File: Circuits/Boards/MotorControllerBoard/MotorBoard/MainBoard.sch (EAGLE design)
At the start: 90 parts, among them M1 IRFS7537PBF, M2 IRFS7537PBF, M3 IRFS7537PBF, M4 IRFS7537PBF, M5 IRFS7537PBF, M6 IRFS7537PBF, M7 IRFS7537PBF, M8 IRFS7537PBF, Q1 2N3904, Q10 2N3904, Q11 2N3904, Q12 2N3904, Q13 2N3904, Q14 2N3904, Q15 2N3904, Q16 2N3904, Q2 2N3904, Q3 2N3904, Q4 2N3904, Q5 2N3904, Q6 2N3904, Q7 2N3904, Q8 2N3904, Q9 2N3904

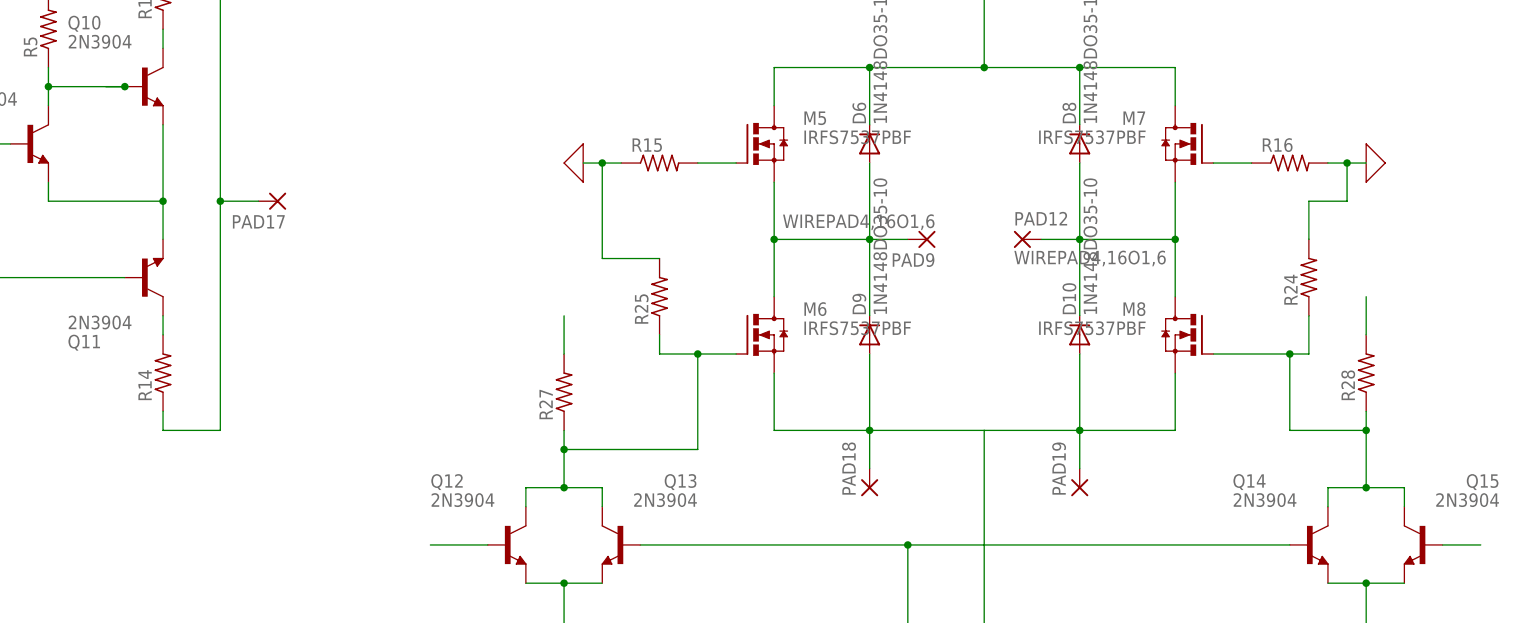
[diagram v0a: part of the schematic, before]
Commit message: Single board, two motor update
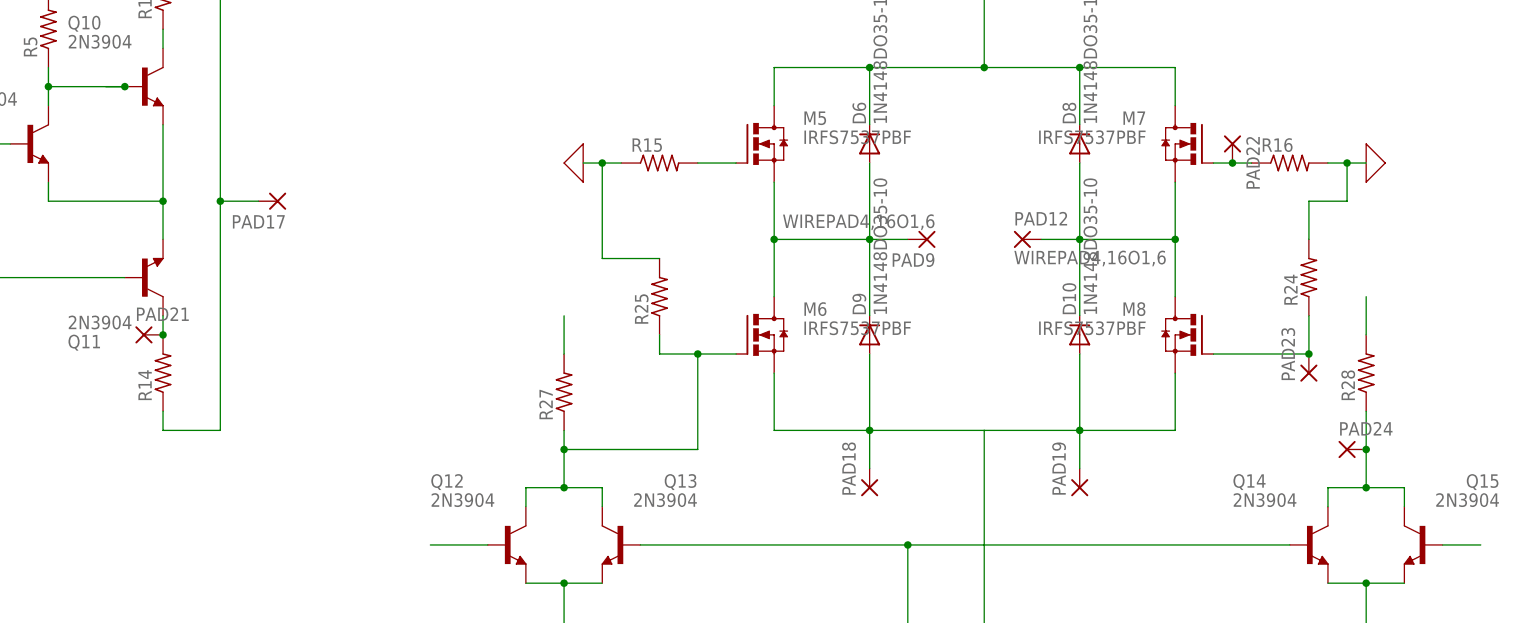
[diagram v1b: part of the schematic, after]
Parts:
- added PAD21, PAD22, PAD23, PAD24: (no value), wirepad:2,54/1,1
- R14, R15, R25: device rcl:R-US_0207/7 -> resistor:R-US_0207/7
- R16, R24: device rcl:R-US_0207/7 -> resistor:R-US_0207/12
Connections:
- removed net BF1: M7.G, Q11.C, R14.2, R16.1
- new net BFF: PAD21.P, Q11.C, R14.2
- new net BFG: M7.G, PAD22.P, R16.1
- new net N$1: M8.G, PAD23.P, R24.1
- net N$5: now also PAD24.P; no longer M8.G, R24.1
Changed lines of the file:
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@@
 <part name="R5" library="rcl" library_urn="urn:adsk.eagle:library:334" deviceset="R-US_" device="0207/7" package3d_urn="urn:adsk.eagle:package:23493/1"/>
 <part name="R13" library="rcl" library_urn="urn:adsk.eagle:library:334" deviceset="R-US_" device="0207/7" package3d_urn="urn:adsk.eagle:package:23493/1"/>
-<part name="R14" library="rcl" library_urn="urn:adsk.eagle:library:334" deviceset="R-US_" device="0207/7" package3d_urn="urn:adsk.eagle:package:23493/1"/>
-<part name="R15" library="rcl" library_urn="urn:adsk.eagle:library:334" deviceset="R-US_" device="0207/7" package3d_urn="urn:adsk.eagle:package:23493/1"/>
-<part name="R16" library="rcl" library_urn="urn:adsk.eagle:library:334" deviceset="R-US_" device="0207/7" package3d_urn="urn:adsk.eagle:package:23493/1"/>
-<part name="R24" library="rcl" library_urn="urn:adsk.eagle:library:334" deviceset="R-US_" device="0207/7" package3d_urn="urn:adsk.eagle:package:23493/1"/>
-<part name="R25" library="rcl" library_urn="urn:adsk.eagle:library:334" deviceset="R-US_" device="0207/7" package3d_urn="urn:adsk.eagle:package:23493/1"/>
+<part name="R14" library="resistor" library_urn="urn:adsk.eagle:library:348" deviceset="R-US_" device="0207/7" package3d_urn="urn:adsk.eagle:package:25942/1"/>
+<part name="R15" library="resistor" library_urn="urn:adsk.eagle:library:348" deviceset="R-US_" device="0207/7" package3d_urn="urn:adsk.eagle:package:25942/1"/>
+<part name="R16" library="resistor" library_urn="urn:adsk.eagle:library:348" deviceset="R-US_" device="0207/12" package3d_urn="urn:adsk.eagle:package:25938/1"/>
+<part name="R24" library="resistor" library_urn="urn:adsk.eagle:library:348" deviceset="R-US_" device="0207/12" package3d_urn="urn:adsk.eagle:package:25938/1"/>
+<part name="R25" library="resistor" library_urn="urn:adsk.eagle:library:348" deviceset="R-US_" device="0207/7" package3d_urn="urn:adsk.eagle:package:25942/1"/>
 <part name="R26" library="rcl" library_urn="urn:adsk.eagle:library:334" deviceset="R-US_" device="0207/7" package3d_urn="urn:adsk.eagle:package:23493/1"/>
 <part name="R27" library="rcl" library_urn="urn:adsk.eagle:library:334" deviceset="R-US_" device="0207/7" package3d_urn="urn:adsk.eagle:package:23493/1"/>
@@
 <part name="PAD19" library="wirepad" library_urn="urn:adsk.eagle:library:412" deviceset="3,81/1,4" device="" package3d_urn="urn:adsk.eagle:package:30835/1"/>
 <part name="PAD20" library="wirepad" library_urn="urn:adsk.eagle:library:412" deviceset="3,81/1,4" device="" package3d_urn="urn:adsk.eagle:package:30835/1"/>
+<part name="PAD21" library="wirepad" library_urn="urn:adsk.eagle:library:412" deviceset="2,54/1,1" device="" package3d_urn="urn:adsk.eagle:package:30836/1"/>
+<part name="PAD22" library="wirepad" library_urn="urn:adsk.eagle:library:412" deviceset="2,54/1,1" device="" package3d_urn="urn:adsk.eagle:package:30836/1"/>
+<part name="PAD23" library="wirepad" library_urn="urn:adsk.eagle:library:412" deviceset="2,54/1,1" device="" package3d_urn="urn:adsk.eagle:package:30836/1"/>
+<part name="PAD24" library="wirepad" library_urn="urn:adsk.eagle:library:412" deviceset="2,54/1,1" device="" package3d_urn="urn:adsk.eagle:package:30836/1"/>
 </parts>
 <sheets>
@@
 <instance part="PAD19" gate="1" x="-157.48" y="81.28" rot="R90"/>
 <instance part="PAD20" gate="1" x="-160.02" y="165.1" rot="R270"/>
+<instance part="PAD21" gate="1" x="-281.94" y="101.6"/>
+<instance part="PAD22" gate="1" x="-137.16" y="127" rot="R270"/>
+<instance part="PAD23" gate="1" x="-127" y="96.52" rot="R90"/>
+<instance part="PAD24" gate="1" x="-121.92" y="86.36"/>
 </instances>
 <busses>
@@
 <wire x1="-119.38" y1="81.28" x2="-114.3" y2="81.28" width="0.1524" layer="91"/>
 <wire x1="-114.3" y1="81.28" x2="-114.3" y2="78.74" width="0.1524" layer="91"/>
-<wire x1="-119.38" y1="91.44" x2="-119.38" y2="88.9" width="0.1524" layer="91"/>
 <junction x="-119.38" y="81.28"/>
-<wire x1="-119.38" y1="88.9" x2="-119.38" y2="81.28" width="0.1524" layer="91"/>
-<wire x1="-129.54" y1="88.9" x2="-129.54" y2="99.06" width="0.1524" layer="91"/>
-<wire x1="-119.38" y1="88.9" x2="-129.54" y2="88.9" width="0.1524" layer="91"/>
-<junction x="-119.38" y="88.9"/>
-<pinref part="M8" gate="G$1" pin="G"/>
-<wire x1="-139.7" y1="99.06" x2="-129.54" y2="99.06" width="0.1524" layer="91"/>
+<wire x1="-119.38" y1="91.44" x2="-119.38" y2="86.36" width="0.1524" layer="91"/>
 <pinref part="R28" gate="G$1" pin="1"/>
-<wire x1="-129.54" y1="99.06" x2="-127" y2="99.06" width="0.1524" layer="91"/>
-<junction x="-129.54" y="99.06"/>
-<wire x1="-127" y1="99.06" x2="-127" y2="104.14" width="0.1524" layer="91"/>
-<pinref part="R24" gate="G$1" pin="1"/>
+<pinref part="PAD24" gate="1" pin="P"/>
+<wire x1="-119.38" y1="86.36" x2="-119.38" y2="81.28" width="0.1524" layer="91"/>
+<junction x="-119.38" y="86.36"/>
 </segment>
 </net>
@@
 </segment>
 </net>
-<net name="BF1" class="0">
+<net name="BFG" class="0">
 <segment>
 <pinref part="M7" gate="G$1" pin="G"/>
-<wire x1="-139.7" y1="124.46" x2="-134.62" y2="124.46" width="0.1524" layer="91"/>
+<wire x1="-139.7" y1="124.46" x2="-137.16" y2="124.46" width="0.1524" layer="91"/>
 <pinref part="R16" gate="G$1" pin="1"/>
-</segment>
-<segment>
-<pinref part="Q11" gate="G1" pin="C"/>
-<wire x1="-279.4" y1="101.6" x2="-279.4" y2="104.14" width="0.1524" layer="91"/>
-<pinref part="R14" gate="G$1" pin="2"/>
+<pinref part="PAD22" gate="1" pin="P"/>
+<wire x1="-137.16" y1="124.46" x2="-134.62" y2="124.46" width="0.1524" layer="91"/>
+<junction x="-137.16" y="124.46"/>
 </segment>
 </net>
@@
 </segment>
 </net>
+<net name="BFF" class="0">
+<segment>
+<pinref part="Q11" gate="G1" pin="C"/>
+<wire x1="-279.4" y1="101.6" x2="-279.4" y2="104.14" width="0.1524" layer="91"/>
+<pinref part="R14" gate="G$1" pin="2"/>
+<pinref part="PAD21" gate="1" pin="P"/>
+<junction x="-279.4" y="101.6"/>
+</segment>
+</net>
+<net name="N$1" class="0">
+<segment>
+<pinref part="M8" gate="G$1" pin="G"/>
+<wire x1="-139.7" y1="99.06" x2="-127" y2="99.06" width="0.1524" layer="91"/>
+<wire x1="-127" y1="99.06" x2="-127" y2="104.14" width="0.1524" layer="91"/>
+<pinref part="R24" gate="G$1" pin="1"/>
+<pinref part="PAD23" gate="1" pin="P"/>
+<junction x="-127" y="99.06"/>
+</segment>
+</net>
